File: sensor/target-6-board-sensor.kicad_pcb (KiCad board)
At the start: 2 copper layers, 33 x 33 mm, 8 parts, among them J1 RJ25

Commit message: sensor: change buzzer to 15mm from 12mm
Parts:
- BZ1: footprint Buzzer_Beeper:Buzzer_12x9.5RM7.6 -> Buzzer_Beeper:Buzzer_15x7.5RM7.6
- moved D1 5.08 mm to (54.6, 44.5)
- moved BZ1 2.84 mm to (43.2, 33.0)
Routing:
- net Net-(D1-A): track 15.0 -> 9.94 mm
- net Net-(BZ1-+): track 15.5 -> 16.8 mm
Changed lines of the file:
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@@
     )
   )
-  (footprint "Buzzer_Beeper:Buzzer_12x9.5RM7.6" (layer "F.Cu")
-    (at 41.91 30.48)
-    (descr "Generic Buzzer, D12mm height 9.5mm with RM7.6mm")
+  (footprint "Buzzer_Beeper:Buzzer_15x7.5RM7.6" (layer "F.Cu")
+    (at 43.19 33.02)
+    (descr "Generic Buzzer, D15mm height 7.5mm with RM7.6mm")
     (tags "buzzer")
     (property "Sheetfile" "target-6-board-sensor.kicad_sch")
@@
     (property "ki_keywords" "quartz resonator ceramic")
     (attr through_hole)
-    (fp_text reference "BZ1" (at 12.7 0) (layer "F.SilkS")
-        (effects (font (size 1 1) (thickness 0.15)))
-    )
-    (fp_text value "Buzzer" (at 12.7 -2.54) (layer "F.Fab")
+    (fp_text reference "BZ1" (at 3.81 -8.89) (layer "F.SilkS")
+        (effects (font (size 1 1) (thickness 0.15)))
+    )
+    (fp_text value "Buzzer" (at 3.81 8.89) (layer "F.Fab")
         (effects (font (size 1 1) (thickness 0.15)))
     )
@@
         (effects (font (size 1 1) (thickness 0.15)))
     )
+    (fp_text user "${REFERENCE}" (at 3.8 -4) (layer "F.Fab")
+        (effects (font (size 1 1) (thickness 0.15)))
+    )
     (fp_text user "+" (at -0.01 -2.54) (layer "F.Fab")
         (effects (font (size 1 1) (thickness 0.15)))
     )
-    (fp_text user "${REFERENCE}" (at 3.8 -4) (layer "F.Fab")
-        (effects (font (size 1 1) (thickness 0.15)))
-    )
-    (fp_circle (center 3.8 0) (end 9.9 0)
+    (fp_circle (center 3.8 0) (end 11.4 0)
       (stroke (width 0.12) (type solid)) (fill none) (layer "F.SilkS"))
-    (fp_circle (center 3.8 0) (end 10.05 0)
+    (fp_circle (center 3.8 0) (end 11.55 0)
       (stroke (width 0.05) (type solid)) (fill none) (layer "F.CrtYd"))
     (fp_circle (center 3.8 0) (end 4.8 0)
       (stroke (width 0.1) (type solid)) (fill none) (layer "F.Fab"))
-    (fp_circle (center 3.8 0) (end 9.8 0)
+    (fp_circle (center 3.8 0) (end 11.3 0)
       (stroke (width 0.1) (type solid)) (fill none) (layer "F.Fab"))
     (pad "1" thru_hole rect (at 0 0) (size 2 2) (drill 1) (layers "*.Cu" "*.Mask")
@@
     (pad "2" thru_hole circle (at 7.6 0) (size 2 2) (drill 1) (layers "*.Cu" "*.Mask")
       (net 1 "GND") (pinfunction "-") (pintype "passive"))
-    (model "${KICAD6_3DMODEL_DIR}/Buzzer_Beeper.3dshapes/Buzzer_12x9.5RM7.6.wrl"
+    (model "${KICAD6_3DMODEL_DIR}/Buzzer_Beeper.3dshapes/Buzzer_15x7.5RM7.6.wrl"
       (offset (xyz 0 0 0))
       (scale (xyz 1 1 1))
@@
   )
   (footprint "LED_THT:LED_D5.0mm" (layer "F.Cu")
-    (at 54.61 39.37 180)
+    (at 54.61 44.45 180)
     (descr "LED, diameter 5.0mm, 2 pins, http://cdn-reichelt.de/documents/datenblatt/A500/LL-504BC2E-009.pdf")
     (tags "LED diameter 5.0mm 2 pins")
@@
   (gr_rect (start 24.13 17.78) (end 57.15 50.8)
     (stroke (width 0.05) (type default)) (fill none) (layer "Edge.Cuts"))
-  (segment (start 43.18 46.99) (end 43.18 41.91) (width 0.2) (layer "F.Cu") (net 2))
-  (segment (start 43.18 41.91) (end 45.72 39.37) (width 0.2) (layer "F.Cu") (net 2))
-  (segment (start 45.72 39.37) (end 52.07 39.37) (width 0.2) (layer "F.Cu") (net 2))
+  (segment (start 52.07 44.45) (end 45.72 44.45) (width 0.2) (layer "F.Cu") (net 2))
+  (segment (start 45.72 44.45) (end 43.18 46.99) (width 0.2) (layer "F.Cu") (net 2))
   (segment (start 36.83 44.45) (end 34.29 44.45) (width 0.2) (layer "F.Cu") (net 4))
   (segment (start 38.1 43.18) (end 36.83 44.45) (width 0.2) (layer "F.Cu") (net 4))
@@
   (segment (start 31.72 34.66) (end 31.72 33.05) (width 0.2) (layer "F.Cu") (net 5))
   (segment (start 31.72 33.05) (end 33.02 31.75) (width 0.2) (layer "F.Cu") (net 5))
-  (segment (start 41.91 30.48) (end 43.18 30.48) (width 0.2) (layer "F.Cu") (net 6))
-  (segment (start 46.99 26.67) (end 46.99 21.59) (width 0.2) (layer "F.Cu") (net 6))
-  (segment (start 43.18 30.48) (end 46.99 26.67) (width 0.2) (layer "F.Cu") (net 6))
+  (segment (start 46.99 21.59) (end 46.99 29.22) (width 0.2) (layer "F.Cu") (net 6))
   (segment (start 46.99 21.59) (end 43.18 21.59) (width 0.2) (layer "F.Cu") (net 6))
+  (segment (start 46.99 29.22) (end 43.19 33.02) (width 0.2) (layer "F.Cu") (net 6))
   (zone (net 1) (net_name "GND") (layer "F.Cu") (hatch edge 0.5)
     (connect_pads (clearance 0.5))

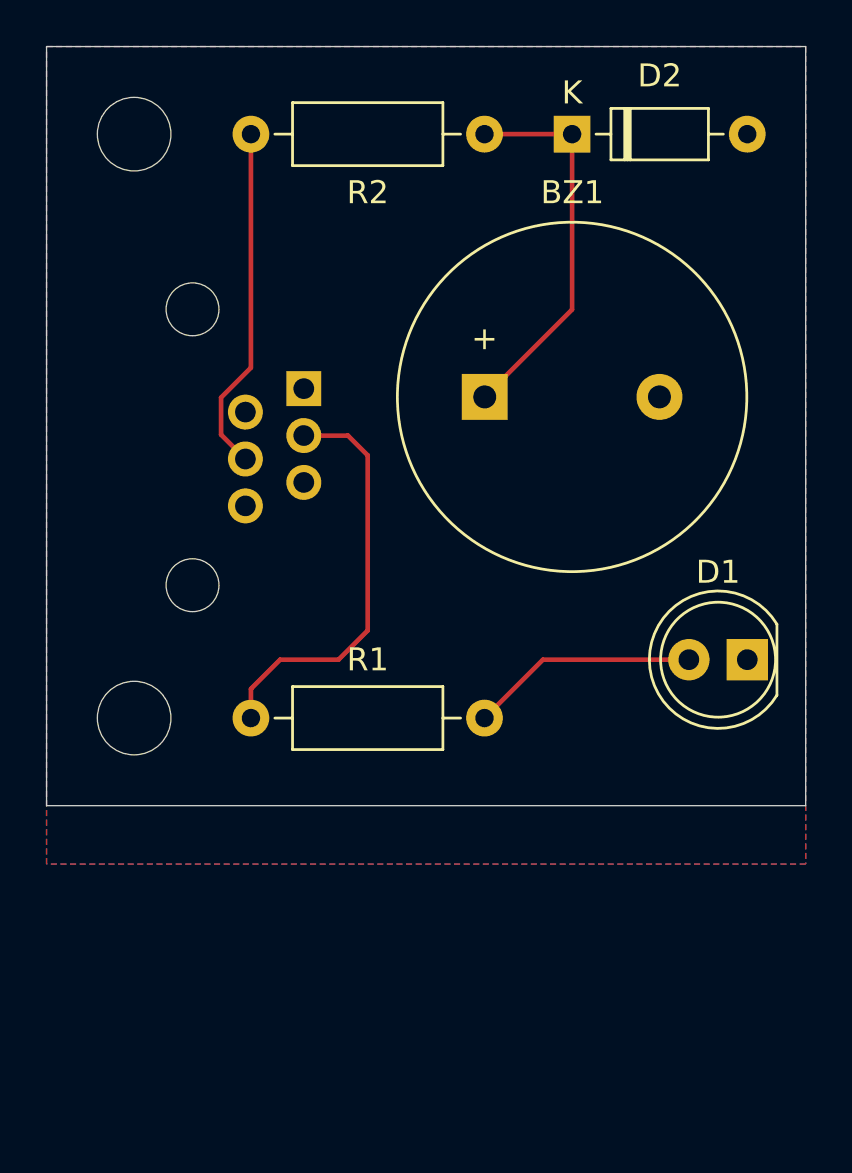
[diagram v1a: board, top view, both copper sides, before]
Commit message: sensor: fix distance of mounting holes
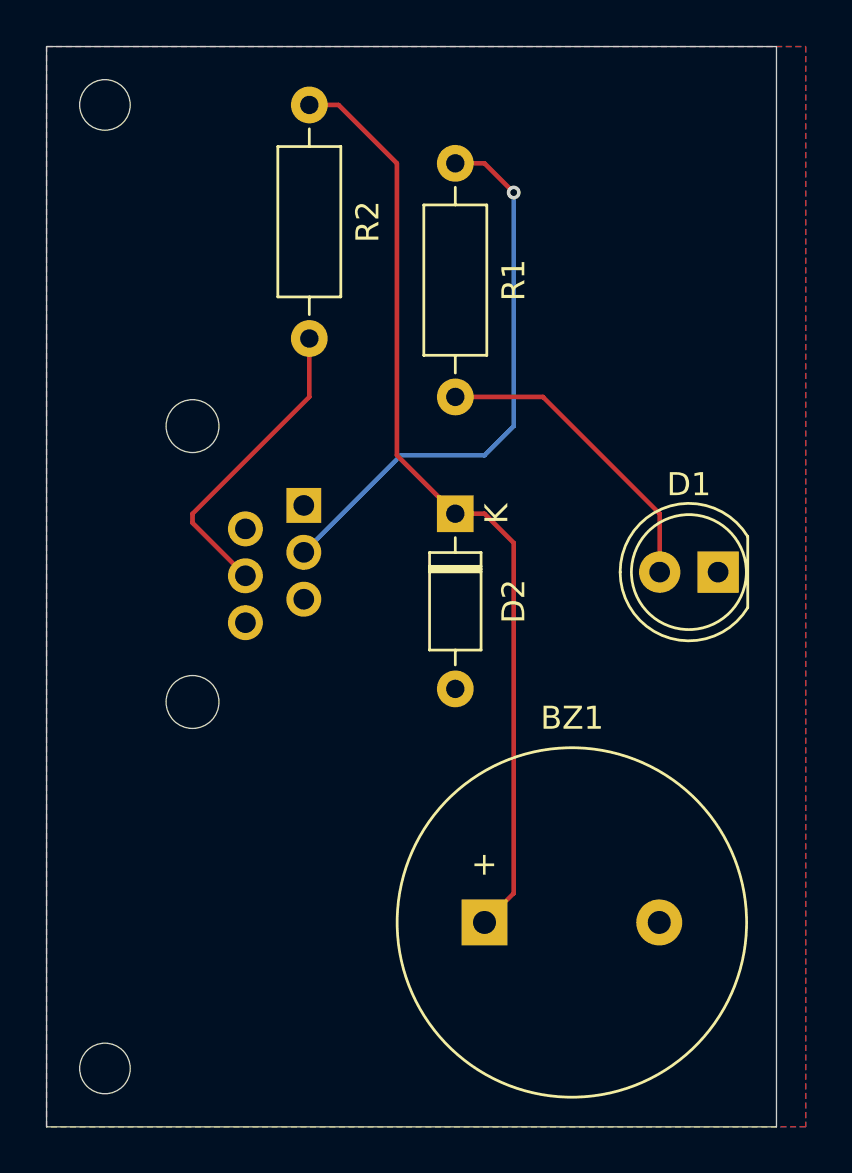
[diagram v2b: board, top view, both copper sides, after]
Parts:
- H1, H2: footprint MountingHole:MountingHole_3.2mm_M3 -> MountingHole:MountingHole_2.2mm_M2
- moved R1 25.7 mm to (41.9, 22.9), turned to -90 degrees
- moved BZ1 22.9 mm to (43.2, 55.9)
- moved D2 17.3 mm to (41.9, 38.1), turned to -90 degrees
- moved H2 15.3 mm to (26.7, 62.2)
- moved R2 9.25 mm to (35.6, 30.5), turned to 90 degrees
- moved J1 5.08 mm to (35.3, 37.7)
- moved D1 4.02 mm to (53.3, 40.6)
- moved H1 1.80 mm to (26.7, 20.3)
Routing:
- net Net-(BZ1-+): track 16.8 -> 41.3 mm
- net TARGET_LED: track 18.2 -> 24.6 mm, vias 0 -> 1
- net Net-(D1-A): track 9.94 -> 13.5 mm
- net SENSOR: track 15.1 -> 13.4 mm
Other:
- board size 33 x 33 mm -> 31.8 x 47 mm

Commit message: sensor: add board name and version
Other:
- board text added: "target-6-sensor v1.0-rc2"
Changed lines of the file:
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@@
   (gr_rect (start 24.13 17.78) (end 55.88 64.77)
     (stroke (width 0.05) (type default)) (fill none) (layer "Edge.Cuts"))
+  (gr_text "target-6-sensor\nv1.0-rc2" (at 54.61 19.05 90) (layer "F.SilkS")
+    (effects (font (size 1 1) (thickness 0.125)) (justify right bottom))
+  )
   (segment (start 50.8 40.64) (end 50.8 38.1) (width 0.2) (layer "F.Cu") (net 2))
   (segment (start 50.8 38.1) (end 45.72 33.02) (width 0.2) (layer "F.Cu") (net 2))
